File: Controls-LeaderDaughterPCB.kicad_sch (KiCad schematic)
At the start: 10 parts

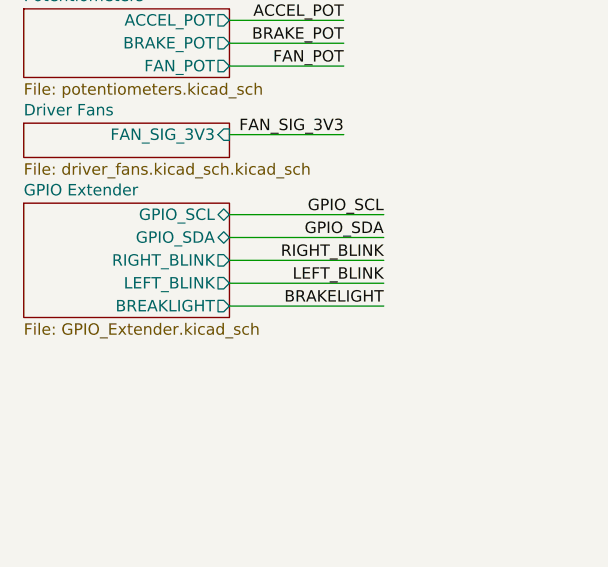
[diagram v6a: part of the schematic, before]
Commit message: assigned footprints
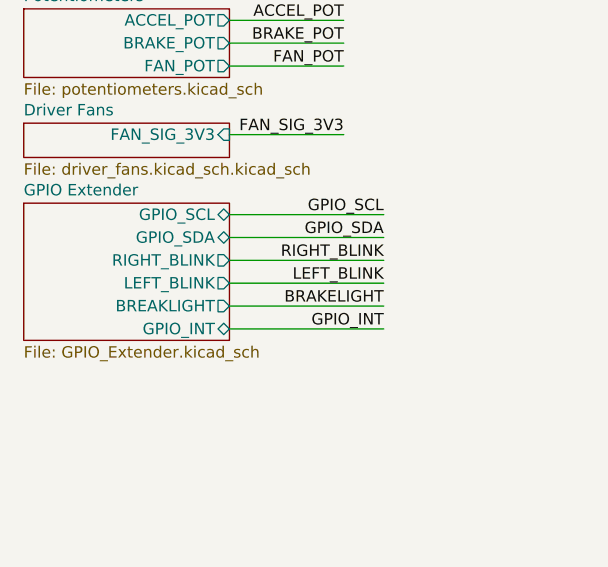
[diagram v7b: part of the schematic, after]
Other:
- sheet GPIO Extender ports: added GPIO_INT; removed none
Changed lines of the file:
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@@
+    (stroke (width 0) (type default))
+  )
+  (wire (pts (xy 35.56 73.025) (xy 52.705 73.025))
     (stroke (width 0) (type default))
   )
@@
   (label "BPS_IG" (at 110.49 50.165 0) (fields_autoplaced)
     (effects (font (size 1.27 1.27)) (justify left bottom))
+  )
+  (label "GPIO_INT" (at 52.705 73.025 180) (fields_autoplaced)
+    (effects (font (size 1.27 1.27)) (justify right bottom))
   )
   (label "BRAKELIGHT" (at 48.26 15.875 180) (fields_autoplaced)
@@
     )
   )
-  (sheet (at 12.7 59.055) (size 22.86 12.7) (fields_autoplaced)
+  (sheet (at 12.7 59.055) (size 22.86 15.24) (fields_autoplaced)
     (stroke (width 0.1524) (type solid))
     (fill (color 0 0 0 0.0000))
@@
       (effects (font (size 1.27 1.27)) (justify left bottom))
     )
-    (property "Sheetfile" "GPIO_Extender.kicad_sch" (at 12.7 72.3396 0)
+    (property "Sheetfile" "GPIO_Extender.kicad_sch" (at 12.7 74.8796 0)
       (effects (font (size 1.27 1.27)) (justify left top))
     )
@@
       (effects (font (size 1.27 1.27)) (justify right))
     )
+    (pin "GPIO_INT" bidirectional (at 35.56 73.025 0)
+      (effects (font (size 1.27 1.27)) (justify right))
+    )

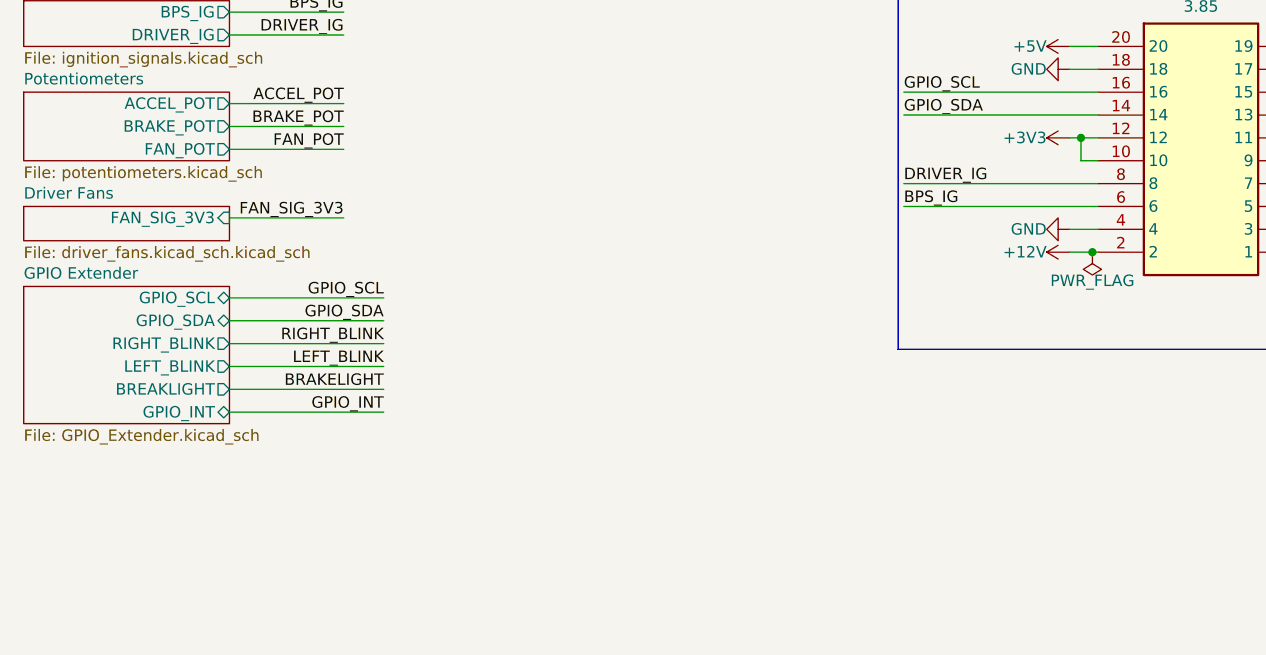
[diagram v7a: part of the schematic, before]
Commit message: organized schematic, changed resistor values, moved ignition signals to IC
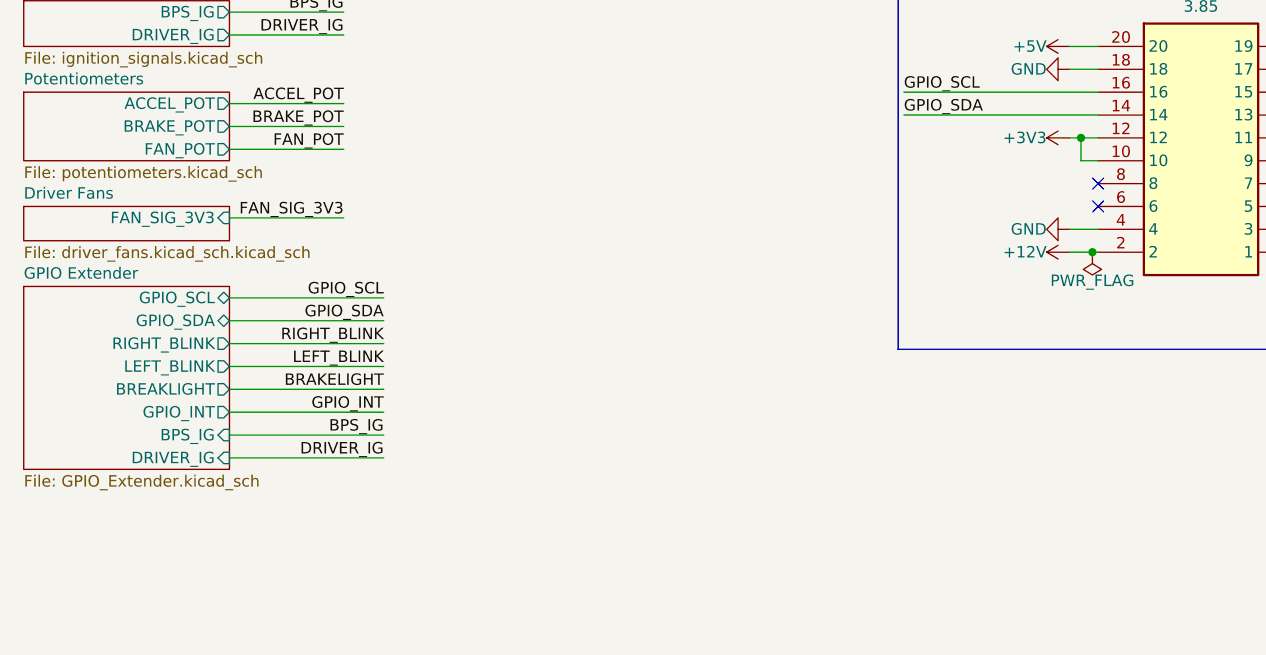
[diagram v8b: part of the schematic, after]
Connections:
- net BPS_IG: no longer SOM1.6
- net DRIVER_IG: no longer SOM1.8
- no-connect marks 5 -> 7
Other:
- sheet GPIO Extender ports: added BPS_IG, DRIVER_IG; removed none
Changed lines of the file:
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@@
   (no_connect (at 154.94 45.085))
   (no_connect (at 154.94 42.545))
+  (no_connect (at 132.08 50.165))
+  (no_connect (at 132.08 47.625))
   (no_connect (at 248.92 51.435))
   (no_connect (at 154.94 47.625))
@@
     (stroke (width 0) (type default))
   )
-  (wire (pts (xy 132.08 47.625) (xy 110.49 47.625))
-    (stroke (width 0) (type default))
-  )
   (wire (pts (xy 226.06 51.435) (xy 204.47 51.435))
     (stroke (width 0) (type default))
@@
     (stroke (width 0) (type default))
   )
+  (wire (pts (xy 35.56 78.105) (xy 52.705 78.105))
+    (stroke (width 0) (type default))
+  )
   (wire (pts (xy 158.115 50.165) (xy 156.845 50.165))
     (stroke (width 0) (type default))
@@
     (stroke (width 0) (type default))
   )
+  (wire (pts (xy 35.56 75.565) (xy 52.705 75.565))
+    (stroke (width 0) (type default))
+  )
   (wire (pts (xy 248.92 41.275) (xy 270.51 41.275))
     (stroke (width 0) (type default))
   )
   (wire (pts (xy 35.56 18.415) (xy 48.26 18.415))
-    (stroke (width 0) (type default))
-  )
-  (wire (pts (xy 132.08 50.165) (xy 110.49 50.165))
     (stroke (width 0) (type default))
   )
@@
     (effects (font (size 1.27 1.27)) (justify right bottom))
   )
-  (label "BPS_IG" (at 110.49 50.165 0) (fields_autoplaced)
-    (effects (font (size 1.27 1.27)) (justify left bottom))
+  (label "DRIVER_IG" (at 52.705 78.105 180) (fields_autoplaced)
+    (effects (font (size 1.27 1.27)) (justify right bottom))
   )
   (label "GPIO_INT" (at 52.705 73.025 180) (fields_autoplaced)
@@
     (effects (font (size 1.27 1.27)) (justify right bottom))
   )
-  (label "DRIVER_IG" (at 110.49 47.625 0) (fields_autoplaced)
-    (effects (font (size 1.27 1.27)) (justify left bottom))
-  )
   (label "RIGHT_BLINK" (at 48.26 20.955 180) (fields_autoplaced)
+    (effects (font (size 1.27 1.27)) (justify right bottom))
+  )
+  (label "BPS_IG" (at 52.705 75.565 180) (fields_autoplaced)
     (effects (font (size 1.27 1.27)) (justify right bottom))
   )
@@
     )
   )
-  (sheet (at 12.7 59.055) (size 22.86 15.24) (fields_autoplaced)
+  (sheet (at 12.7 59.055) (size 22.86 20.32) (fields_autoplaced)
     (stroke (width 0.1524) (type solid))
     (fill (color 0 0 0 0.0000))
@@
       (effects (font (size 1.27 1.27)) (justify left bottom))
     )
-    (property "Sheetfile" "GPIO_Extender.kicad_sch" (at 12.7 74.8796 0)
+    (property "Sheetfile" "GPIO_Extender.kicad_sch" (at 12.7 79.9596 0)
       (effects (font (size 1.27 1.27)) (justify left top))
     )
@@
       (effects (font (size 1.27 1.27)) (justify right))
     )
-    (pin "GPIO_INT" bidirectional (at 35.56 73.025 0)
-      (effects (font (size 1.27 1.27)) (justify right))
-    )
+    (pin "GPIO_INT" output (at 35.56 73.025 0)
+      (effects (font (size 1.27 1.27)) (justify right))
+    )
+    (pin "BPS_IG" input (at 35.56 75.565 0)
+      (effects (font (size 1.27 1.27)) (justify right))
+    )
+    (pin "DRIVER_IG" input (at 35.56 78.105 0)
+      (effects (font (size 1.27 1.27)) (justify right))
+    )
